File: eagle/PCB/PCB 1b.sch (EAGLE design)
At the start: 25 parts

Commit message: PCB Work
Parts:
- added AUD, SER: (no value), SparkFun-Connectors:CONN_01
- added J1: 0446200001, con-molex:0446200001
- added J2: AUDIO_JACK_3.5MM_KIT, SparkFun-Connectors:AUDIO_JACK_3.5MM_KIT
- added X2: 0446200002, con-molex:0446200002
- BUZZ: value F/CM12P -> BUZZER-PTH; device buzzer:F/CM12P -> SparkFun-Electromechanical:BUZZER-PTH
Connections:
- net N$6 renamed 8VG
- net N$7 renamed 8V
- new net AUD: 3.5MM.3, 3.5MM.4, AUD.1, RJ45.5
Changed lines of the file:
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@@
 <parts>
 <part name="RJ45" library="con-kycon" library_urn="urn:adsk.eagle:library:157" deviceset="GLX-S-88M" device="" package3d_urn="urn:adsk.eagle:package:7680/1"/>
-<part name="BUZZ" library="buzzer" library_urn="urn:adsk.eagle:library:113" deviceset="F/CM12P" device="" package3d_urn="urn:adsk.eagle:package:5265/1">
+<part name="BUZZ" library="SparkFun-Electromechanical" library_urn="urn:adsk.eagle:library:516" deviceset="BUZZER" device="-PTH" package3d_urn="urn:adsk.eagle:package:38558/1">
 <attribute name="SPICEPREFIX" value="X"/>
 </part>
@@
 <part name="ARD-SERVICE" library="SparkFun-Connectors" library_urn="urn:adsk.eagle:library:513" deviceset="EM406" device="" package3d_urn="urn:adsk.eagle:package:38023/1"/>
 <part name="OSD-SERVICE" library="SparkFun-Connectors" library_urn="urn:adsk.eagle:library:513" deviceset="EM406" device="" package3d_urn="urn:adsk.eagle:package:38023/1"/>
+<part name="SER" library="SparkFun-Connectors" library_urn="urn:adsk.eagle:library:513" deviceset="CONN_01" device="" package3d_urn="urn:adsk.eagle:package:38028/1"/>
+<part name="AUD" library="SparkFun-Connectors" library_urn="urn:adsk.eagle:library:513" deviceset="CONN_01" device="" package3d_urn="urn:adsk.eagle:package:38028/1"/>
+<part name="X2" library="con-molex" library_urn="urn:adsk.eagle:library:165" deviceset="0446200002" device=""/>
+<part name="J1" library="con-molex" library_urn="urn:adsk.eagle:library:165" deviceset="0446200001" device="" value="0446200001"/>
+<part name="J2" library="SparkFun-Connectors" library_urn="urn:adsk.eagle:library:513" deviceset="AUDIO_JACK_3.5MM" device="_KIT" package3d_urn="urn:adsk.eagle:package:38014/1"/>
 </parts>
 <sheets>
@@
 <instance part="ARD-SERVICE" gate="G$1" x="182.88" y="17.78" rot="MR270"/>
 <instance part="OSD-SERVICE" gate="G$1" x="289.56" y="226.06" rot="R90"/>
+<instance part="SER" gate="G$1" x="226.06" y="175.26" rot="R90"/>
+<instance part="AUD" gate="G$1" x="104.14" y="50.8" rot="R90"/>
+<instance part="X2" gate="P" x="157.48" y="276.86"/>
+<instance part="J1" gate="P" x="88.9" y="248.92"/>
+<instance part="J2" gate="G$1" x="127" y="231.14"/>
 </instances>
 <busses>
@@
 <junction x="144.78" y="63.5"/>
 <pinref part="BUZZ" gate="G$1" pin="2"/>
-<wire x1="243.84" y1="91.44" x2="259.08" y2="68.58" width="0.1524" layer="91"/>
+<wire x1="241.3" y1="91.44" x2="259.08" y2="68.58" width="0.1524" layer="91"/>
 <wire x1="259.08" y1="68.58" x2="302.26" y2="68.58" width="0.1524" layer="91"/>
 <junction x="302.26" y="68.58"/>
@@
 <segment>
 <pinref part="BUZZ" gate="G$1" pin="1"/>
-<wire x1="236.22" y1="91.44" x2="223.52" y2="111.76" width="0.1524" layer="91"/>
+<wire x1="238.76" y1="91.44" x2="223.52" y2="111.76" width="0.1524" layer="91"/>
 <pinref part="U$1" gate="G$1" pin="D9"/>
 <wire x1="200.66" y1="116.84" x2="223.52" y2="116.84" width="0.1524" layer="91"/>
@@
 </segment>
 </net>
-<net name="N$6" class="0">
+<net name="8VG" class="0">
 <segment>
 <pinref part="8V" gate="1" pin="P"/>
@@
 </segment>
 </net>
-<net name="N$7" class="0">
+<net name="8V" class="0">
 <segment>
 <pinref part="GND" gate="1" pin="P"/>
@@
 </segment>
 </net>
+<net name="AUD" class="2">
+<segment>
+<pinref part="AUD" gate="G$1" pin="1"/>
+<wire x1="104.14" y1="58.42" x2="101.6" y2="58.42" width="0.1524" layer="91"/>
+<wire x1="101.6" y1="58.42" x2="101.6" y2="78.74" width="0.1524" layer="91"/>
+<pinref part="3.5MM" gate="G$1" pin="3"/>
+<wire x1="101.6" y1="78.74" x2="96.52" y2="78.74" width="0.1524" layer="91"/>
+<pinref part="3.5MM" gate="G$1" pin="4"/>
+<wire x1="96.52" y1="78.74" x2="88.9" y2="78.74" width="0.1524" layer="91"/>
+<wire x1="88.9" y1="83.82" x2="88.9" y2="78.74" width="0.1524" layer="91"/>
+<junction x="88.9" y="78.74"/>
+<pinref part="RJ45" gate="G$1" pin="5"/>
+<wire x1="88.9" y1="106.68" x2="96.52" y2="106.68" width="0.1524" layer="91"/>
+<wire x1="96.52" y1="106.68" x2="96.52" y2="78.74" width="0.1524" layer="91"/>
+<junction x="96.52" y="78.74"/>
+</segment>
+</net>

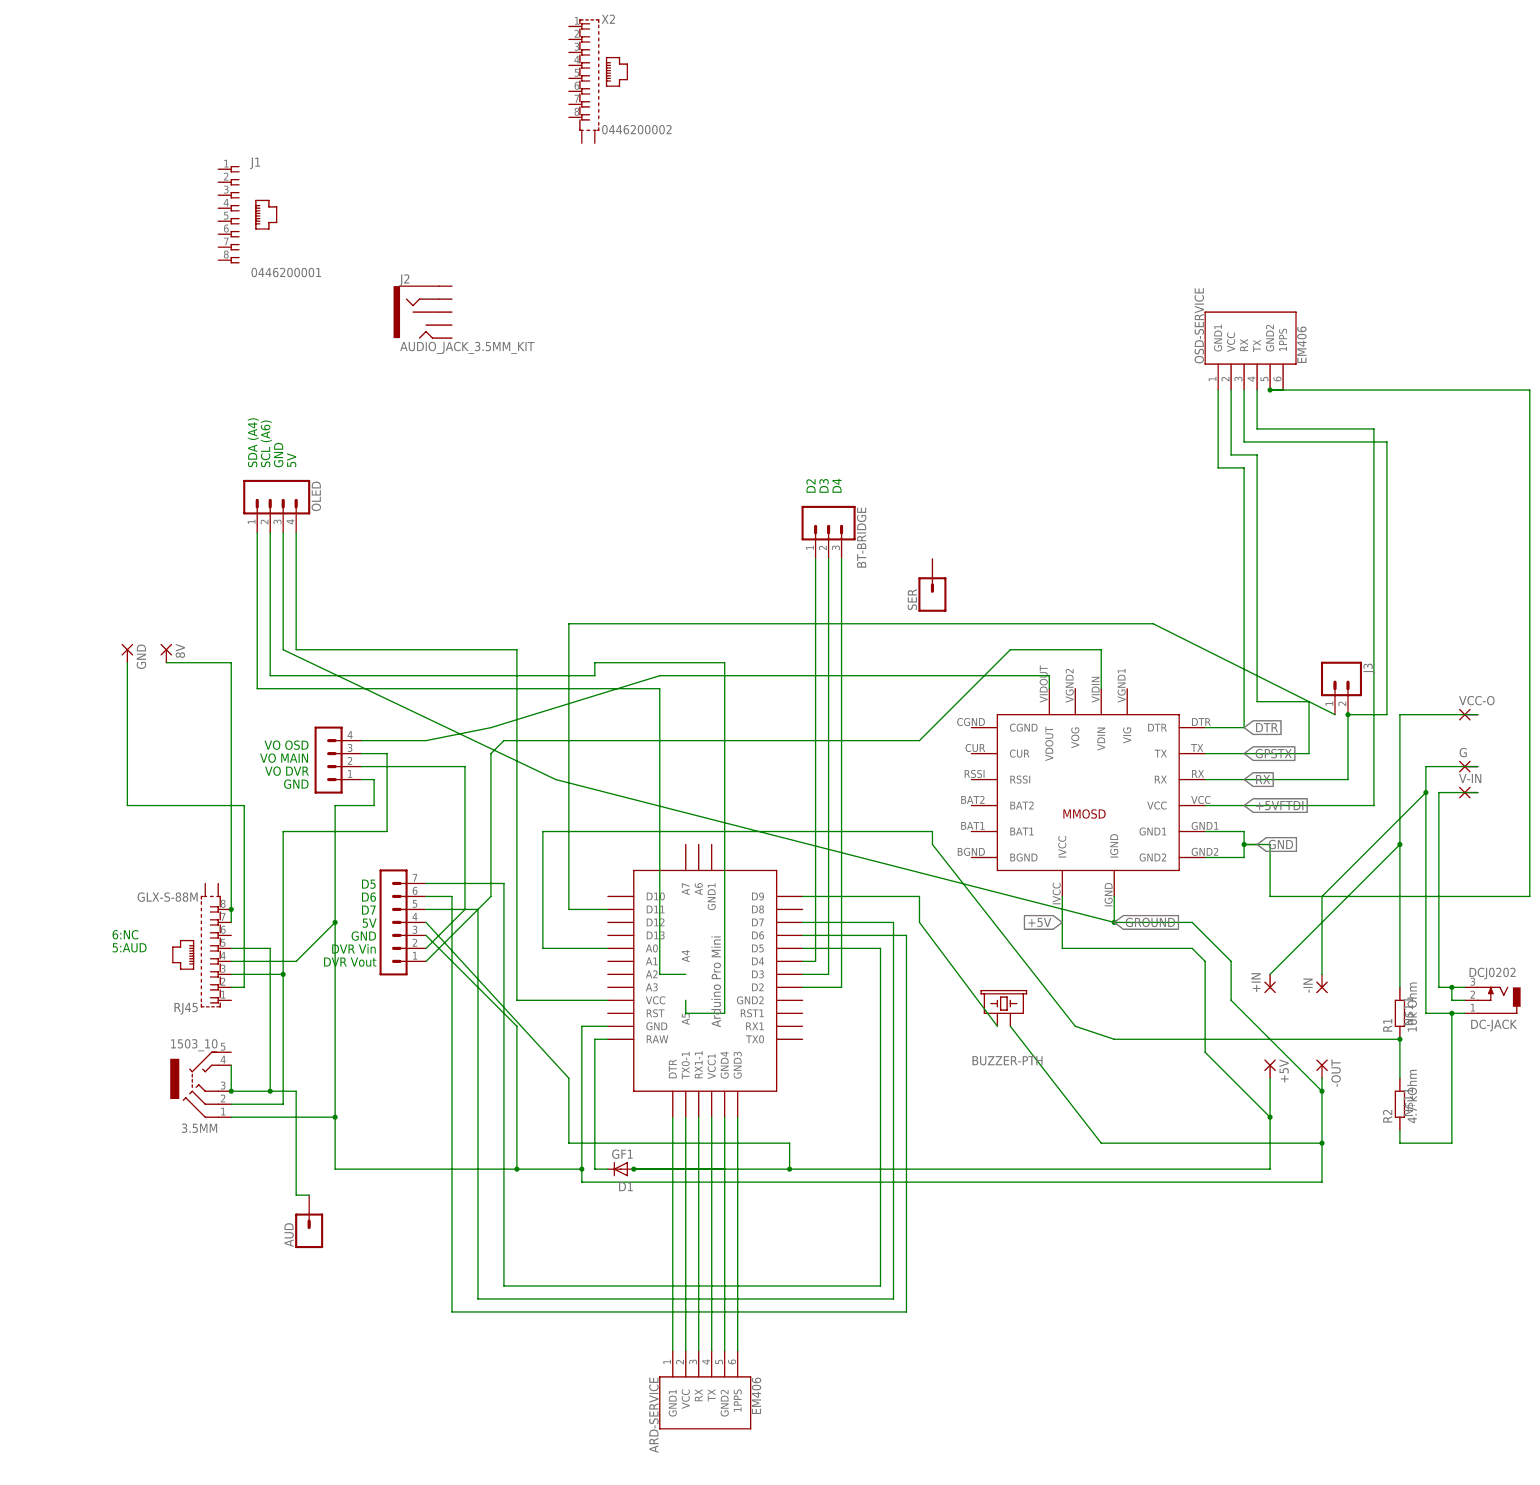
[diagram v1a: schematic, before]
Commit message: Update PCB components
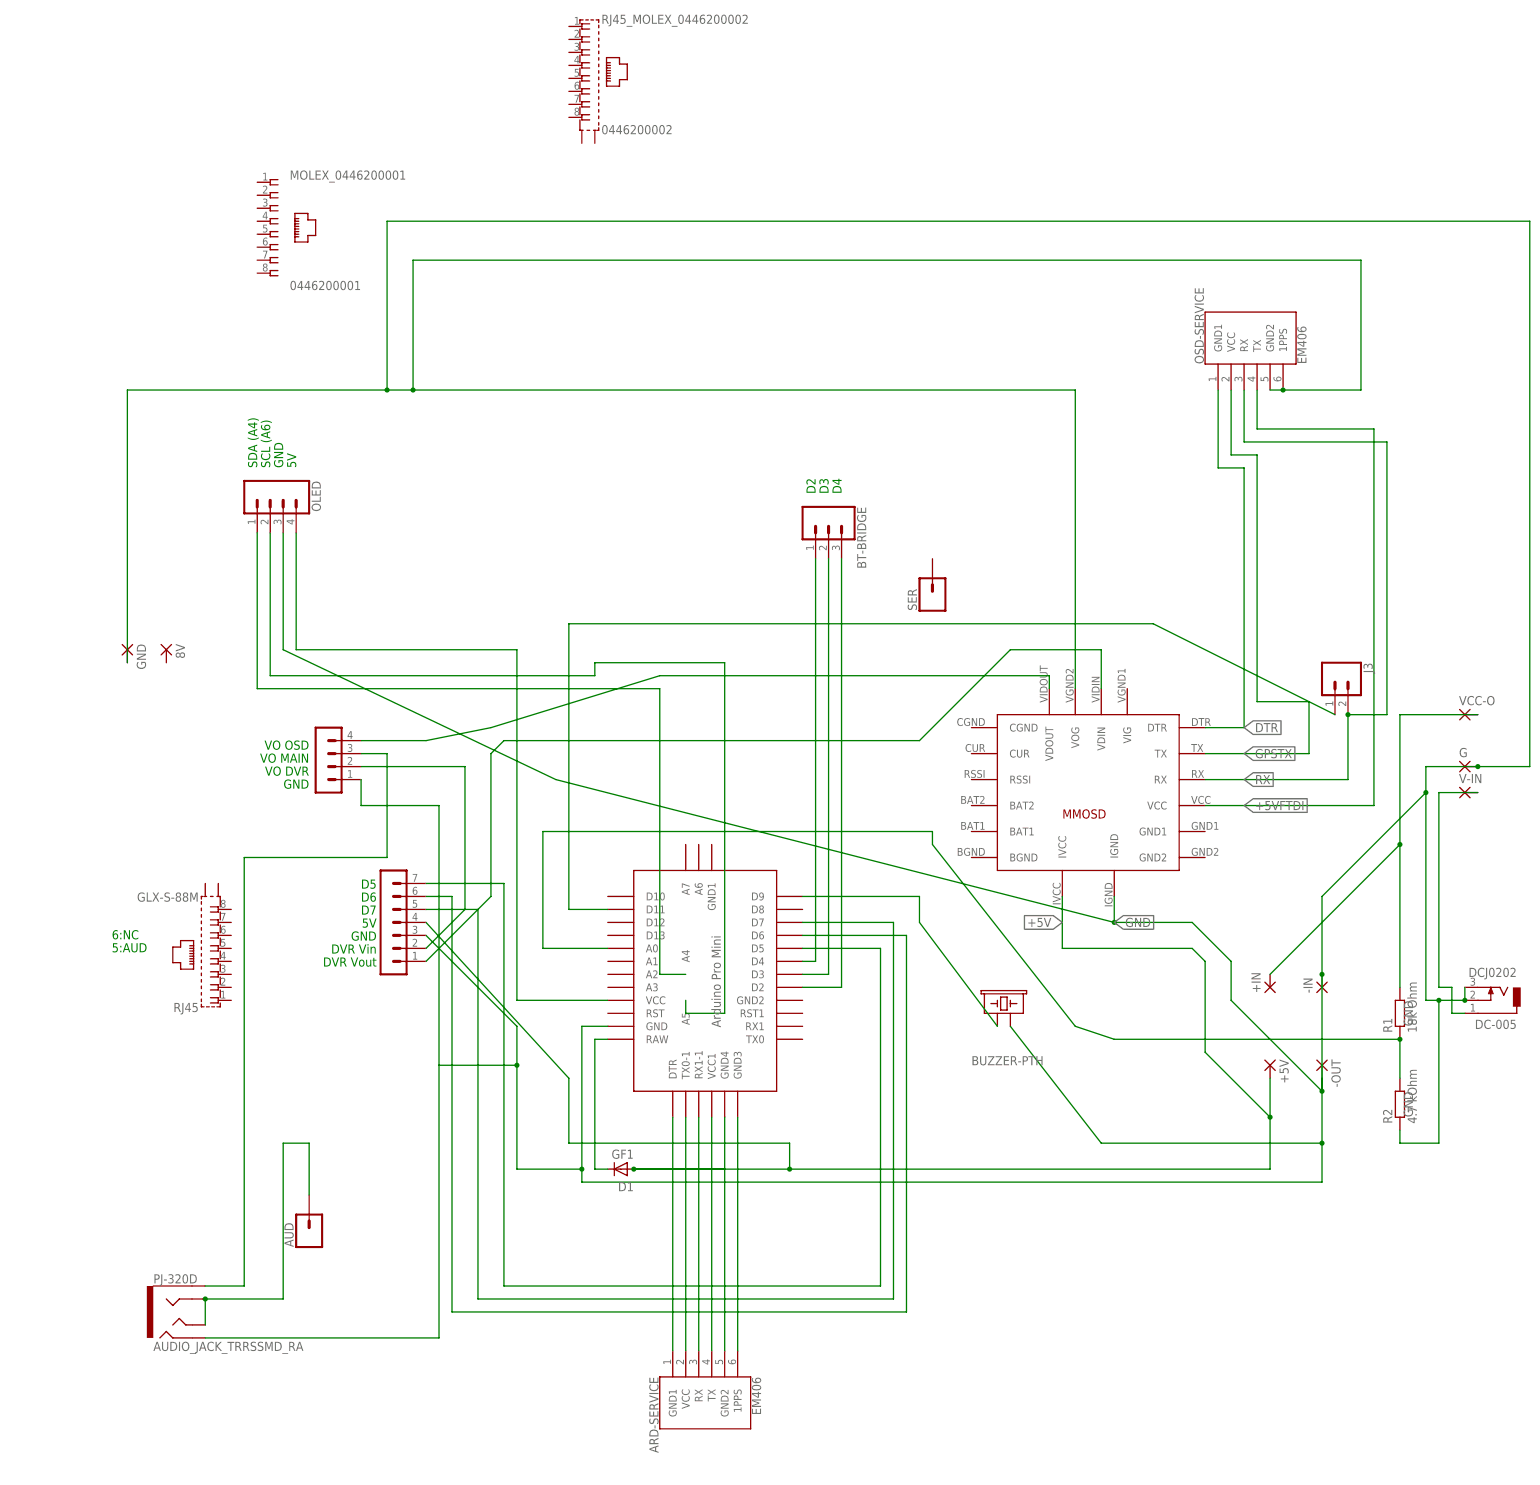
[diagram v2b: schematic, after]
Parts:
- removed 3.5MM: 1503_10, con-lumberg:1503_10
- removed J1: 0446200001, con-molex:0446200001
- removed J2: AUDIO_JACK_3.5MM_KIT, SparkFun-Connectors:AUDIO_JACK_3.5MM_KIT
- added MOLEX_0446200001: 0446200001, con-molex:0446200001
- added PJ-320D: AUDIO_JACK_TRRSSMD_RA, SparkFun-Connectors:AUDIO_JACK_TRRSSMD_RA
- renumbered DC-JACK to DC-005, X2 to RJ45_MOLEX_0446200002
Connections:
- removed net 8V: GND.P, RJ45.2
- removed net 8VG: 8V.P, RJ45.7, RJ45.8
- removed net AUD: 3.5MM.3, 3.5MM.4, AUD.1, RJ45.5
- removed net GROUND: -OUT.P, 3.5MM.1, BUZZ.2, DVR/MODULE-IO.3, MINIMOSD.IGND, OLED.3, RJ45.4, U$1.GND, V-IO.1
- removed net N$11: -IN.P, DC-005.1, G.P, R2.1
- removed net VSIGNAL-A-SW: 3.5MM.2, RJ45.3, V-IO.3
- new net N$3: AUD.1, PJ-320D.RING1, PJ-320D.TIP
- new net N$6: PJ-320D.EARTH, V-IO.3
- net GND: now also -IN.P, -OUT.P, BUZZ.2, DC-005.2, DC-005.3, DVR/MODULE-IO.3, G.P, GND.P, MINIMOSD.IGND, MINIMOSD.VOG, OLED.3, PJ-320D.RING2, R2.1, U$1.GND, V-IO.1; no longer MINIMOSD.GND1, MINIMOSD.GND2
- net N$5: now also DC-005.1; no longer DC-005.2, DC-005.3
